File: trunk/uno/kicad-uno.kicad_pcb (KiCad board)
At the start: 2 copper layers, 57 parts, among them J1 RESET_EN, Q1 FDN340P, SW1 RESET, U1 NCP1117 5V, U2 LP2985-33DBVR, U3 ATMEGA16U2-MU(R), U5 LM358, X2 USB-MINI-AB

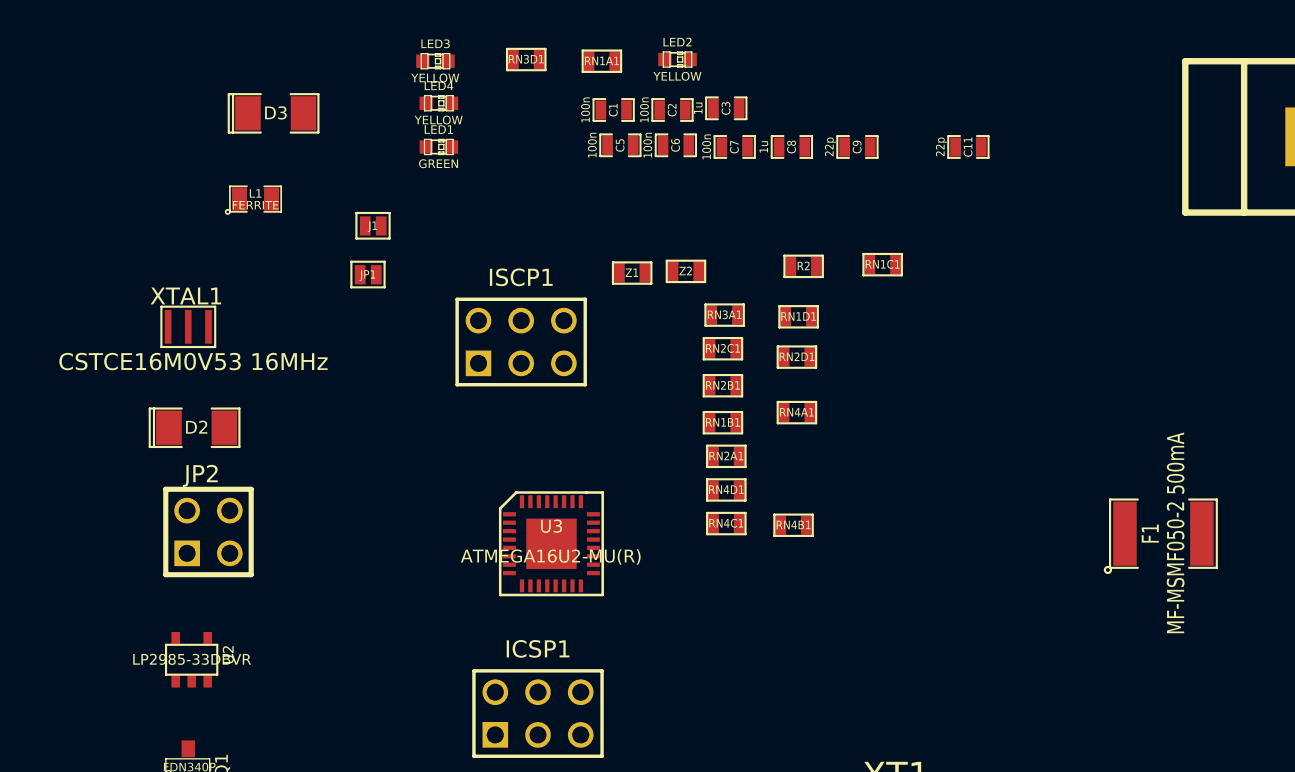
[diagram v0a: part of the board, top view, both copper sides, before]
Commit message: Added resistor network part/module for RN1-4 (no 3D package yet).
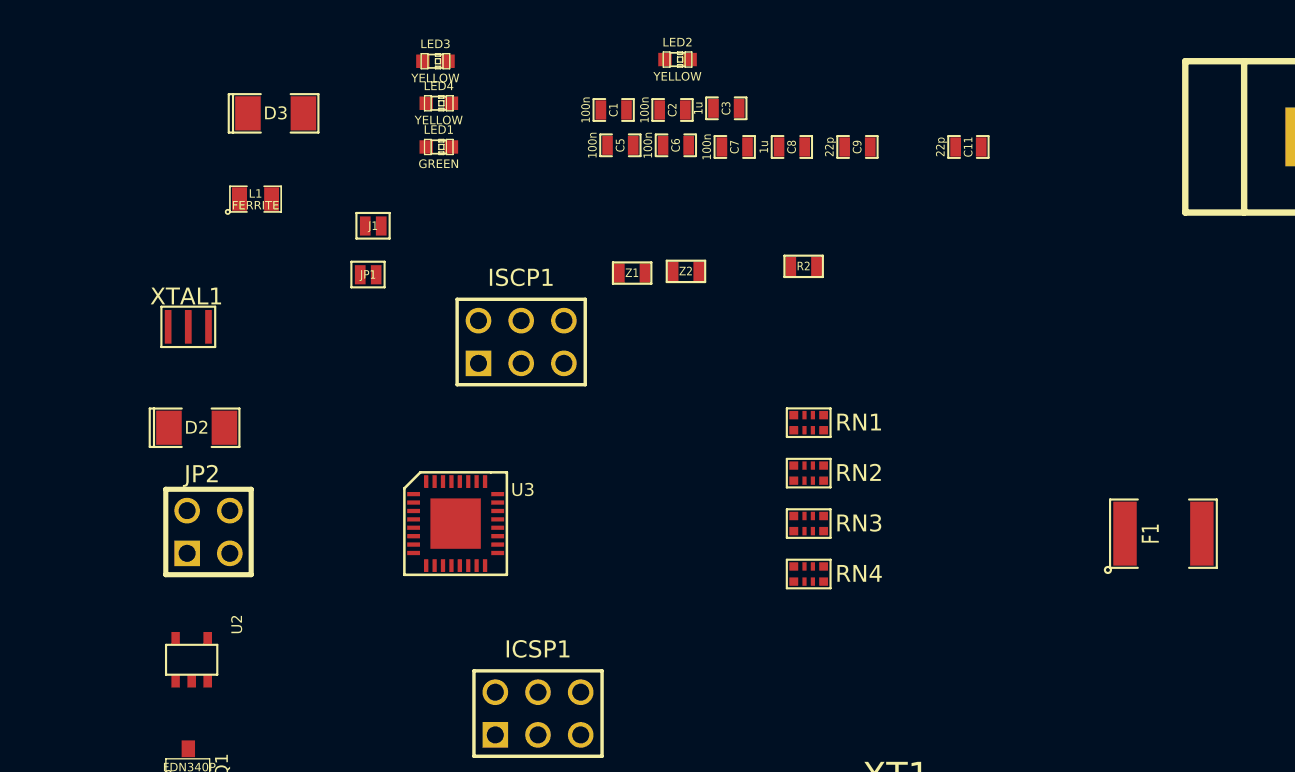
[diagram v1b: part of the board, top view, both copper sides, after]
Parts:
- removed RN1A1, RN1B1, RN1C1, RN1D1: 10K, SM0603
- removed RN2A1, RN2B1, RN2C1, RN2D1, RN4A1, RN4B1, RN4C1, RN4D1: 1K, SM0603
- removed RN3A1, RN3D1: 22R, SM0603
- added RN1: 10K, RN_EXB-28V, F.Cu at (17.0, 15.0)
- added RN2: 1K, RN_EXB-28V, F.Cu at (17.0, 18.0)
- added RN3: 22R, RN_EXB-28V, F.Cu at (17.0, 21.0)
- added RN4: 1K, RN_EXB-28V, F.Cu at (17.0, 24.0)
- moved U3 5.82 mm to (-4.00, 21.0)

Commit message: Board edges completed.
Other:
- board outline added: 68.6 x 53.3 mm
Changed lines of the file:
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@@
     (area 0 0 0 0)
     (thickness 1.6)
-    (drawings 0)
+    (drawings 12)
     (tracks 0)
     (zones 0)
@@
     (trace_min 0.254)
     (segment_width 0.127)
-    (edge_width 0.1)
+    (edge_width 0.254)
     (via_size 0.889)
     (via_drill 0.635)
@@
     (pad_drill 0)
     (pad_to_mask_clearance 0)
-    (aux_axis_origin 0 0)
+    (aux_axis_origin 25.4 25.4)
     (visible_elements 7FFFFBFF)
     (pcbplotparams
@@
     )
   )
+  (gr_arc (start 90.424 77.724) (end 91.44 77.724) (angle 90) (layer Edge.Cuts) (width 0.254))
+  (gr_arc (start 26.416 77.724) (end 26.416 78.74) (angle 90) (layer Edge.Cuts) (width 0.254))
+  (gr_arc (start 26.416 26.416) (end 25.4 26.416) (angle 90) (layer Edge.Cuts) (width 0.254))
+  (gr_line (start 25.4 77.724) (end 25.4 26.416) (angle 90) (layer Edge.Cuts) (width 0.254))
+  (gr_line (start 91.44 26.924) (end 89.916 25.4) (angle 90) (layer Edge.Cuts) (width 0.254))
+  (gr_line (start 91.44 38.354) (end 91.44 26.924) (angle 90) (layer Edge.Cuts) (width 0.254))
+  (gr_line (start 93.98 40.894) (end 91.44 38.354) (angle 90) (layer Edge.Cuts) (width 0.254))
+  (gr_line (start 93.98 73.66) (end 93.98 40.894) (angle 90) (layer Edge.Cuts) (width 0.254))
+  (gr_line (start 91.44 76.2) (end 93.98 73.66) (angle 90) (layer Edge.Cuts) (width 0.254))
+  (gr_line (start 91.44 77.724) (end 91.44 76.2) (angle 90) (layer Edge.Cuts) (width 0.254))
+  (gr_line (start 26.416 25.4) (end 89.916 25.4) (angle 90) (layer Edge.Cuts) (width 0.254))
+  (gr_line (start 26.416 78.74) (end 90.424 78.74) (angle 90) (layer Edge.Cuts) (width 0.254))
 )

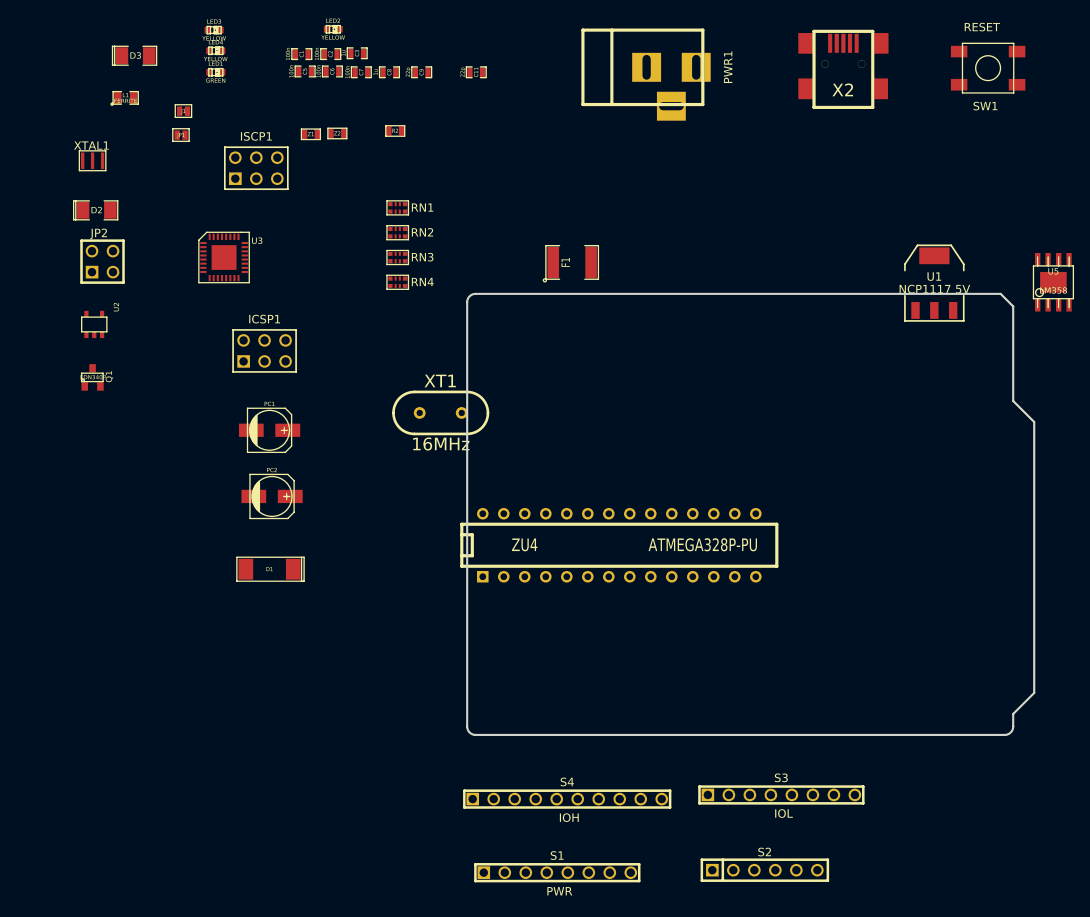
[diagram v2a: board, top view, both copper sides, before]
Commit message: About half the comoponents placed, in the exact same location as the UNO Rev3 reference design, except I changed the USB socket to a mini.
A number of minor schematic errors were corrected, around the pin 
numbering of the four resistor network chips.
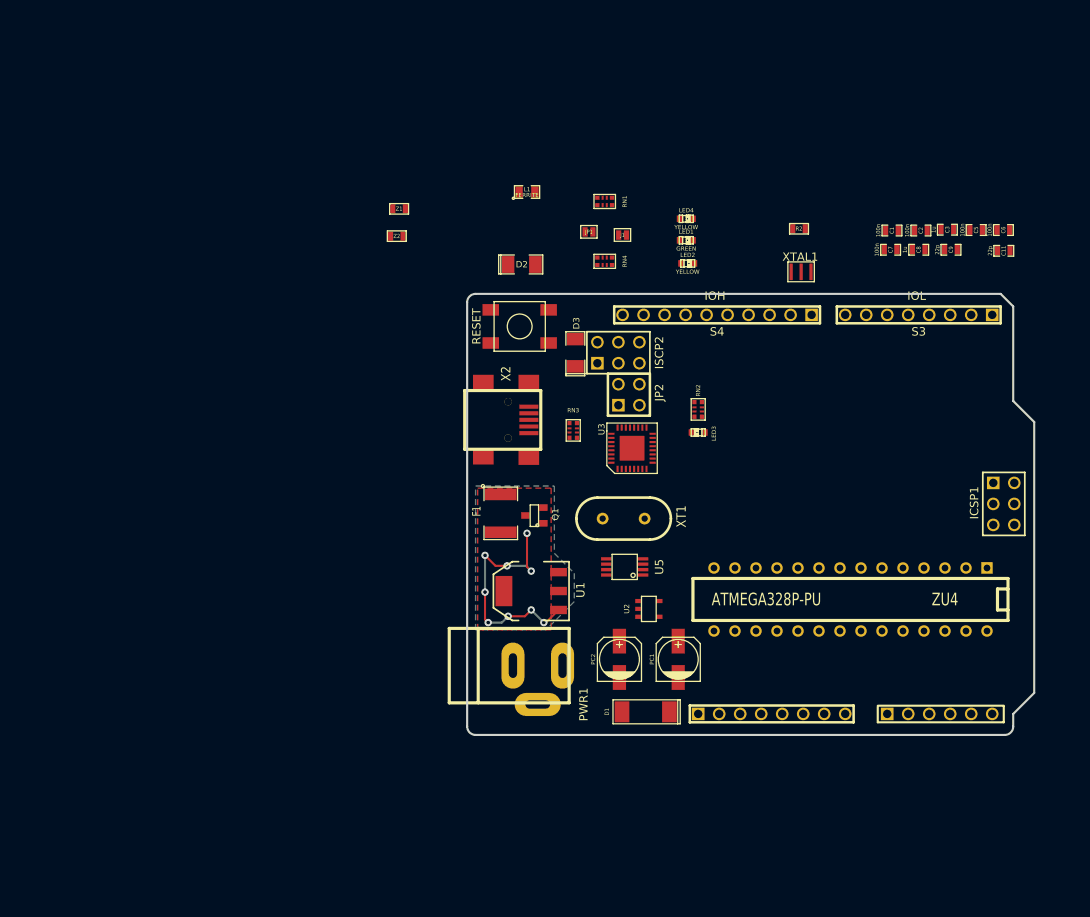
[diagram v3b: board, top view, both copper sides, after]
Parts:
- S2: footprint PIN_ARRAY-6X1 -> pin_array_6x1
- U5: footprint psop-8 -> SSOP8
- moved ICSP1 91.3 mm to (90.3, 50.8), turned to 270 degrees
- moved XTAL1 86.7 mm to (65.8, 22.7)
- moved C5 83.4 mm to (87.0, 17.7)
- moved C6 83.4 mm to (90.3, 17.7)
- moved LED3 76.1 mm to (53.3, 42.2), turned to 180 degrees
- moved U2 75.4 mm to (47.4, 63.5), turned to 270 degrees
- moved C3 74.5 mm to (83.5, 17.6)
- moved C1 74.5 mm to (76.8, 17.7)
- moved C2 74.5 mm to (80.3, 17.7)
- moved PWR1 74.1 mm to (30.7, 70.4)
- moved C7 67.5 mm to (76.6, 20.1)
- moved C9 67.5 mm to (83.9, 20.1)
- moved C8 67.5 mm to (80.0, 20.1)
- moved C11 67.4 mm to (90.3, 20.2)
- moved JP2 65.7 mm to (45.0, 37.6)
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- renumbered ISCP1 to ISCP2
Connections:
- PWR1 pad 1: GND -> N-0000040
- PWR1 pad 2: N-0000040 -> GND
- RN1 pad 1: VIN -> /POWER/CMP
- RN1 pad 3: /POWER/CMP -> +5V
- RN1 pad 4: GND -> /RESET
- RN1 pad 7: +5V -> GND
- RN1 pad 8: /RESET -> VIN
- RN2 pad 1: N-0000036 -> N-0000035
- RN2 pad 2: N-0000035 -> +5V
- RN2 pad 3: N-0000041 -> +5V
- RN2 pad 4: +5V -> DTR
- RN2 pad 5: N-0000042 -> GND
- RN2 pad 6: +5V -> N-0000042
- RN2 pad 7: DTR -> N-0000041
- RN2 pad 8: GND -> N-0000036
- RN3 pad 1: /USB/D- -> N-0000069
- RN3 pad 2: N-0000069 -> (no net)
- RN3 pad 4: (no net) -> N-0000068
- RN3 pad 5: (no net) -> /USB/D+
- RN3 pad 7: /USB/D+ -> (no net)
- RN3 pad 8: N-0000068 -> /USB/D-
- RN4 pad 2: TXD -> /IO0
- RN4 pad 3: /IO0 -> +5V
- RN4 pad 4: RXD -> +5V
- RN4 pad 5: +5V -> N-0000038
- RN4 pad 7: +5V -> RXD
- RN4 pad 8: N-0000038 -> TXD
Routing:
- net GND: track 0.00 -> 29.8 mm, vias 0 -> 9
- added copper zone on B.Cu, net GND
- added copper zone on F.Cu, net GND
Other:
- net class Default: clearance 0.254 -> 0.2032
- rule trace_clearance: 0.254 -> 0.2032

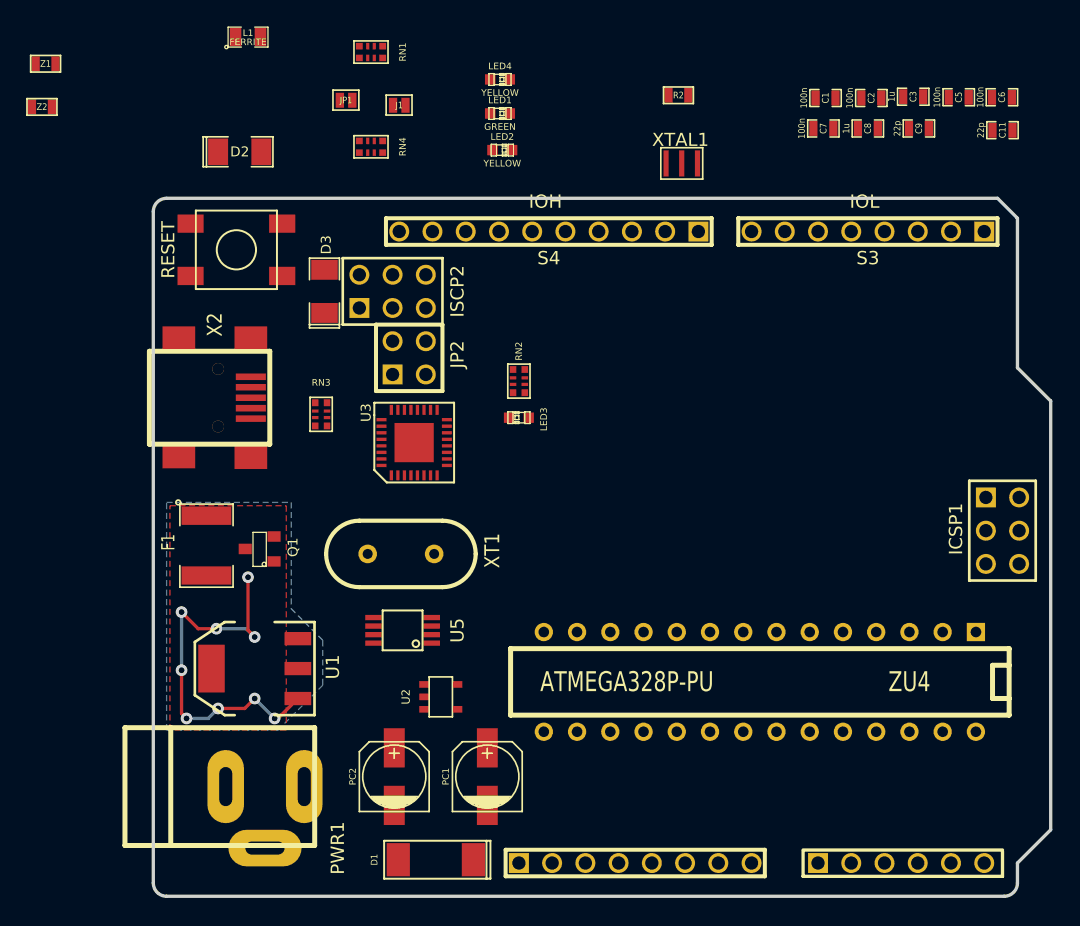
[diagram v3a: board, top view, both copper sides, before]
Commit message: All components placed. Some routing started.
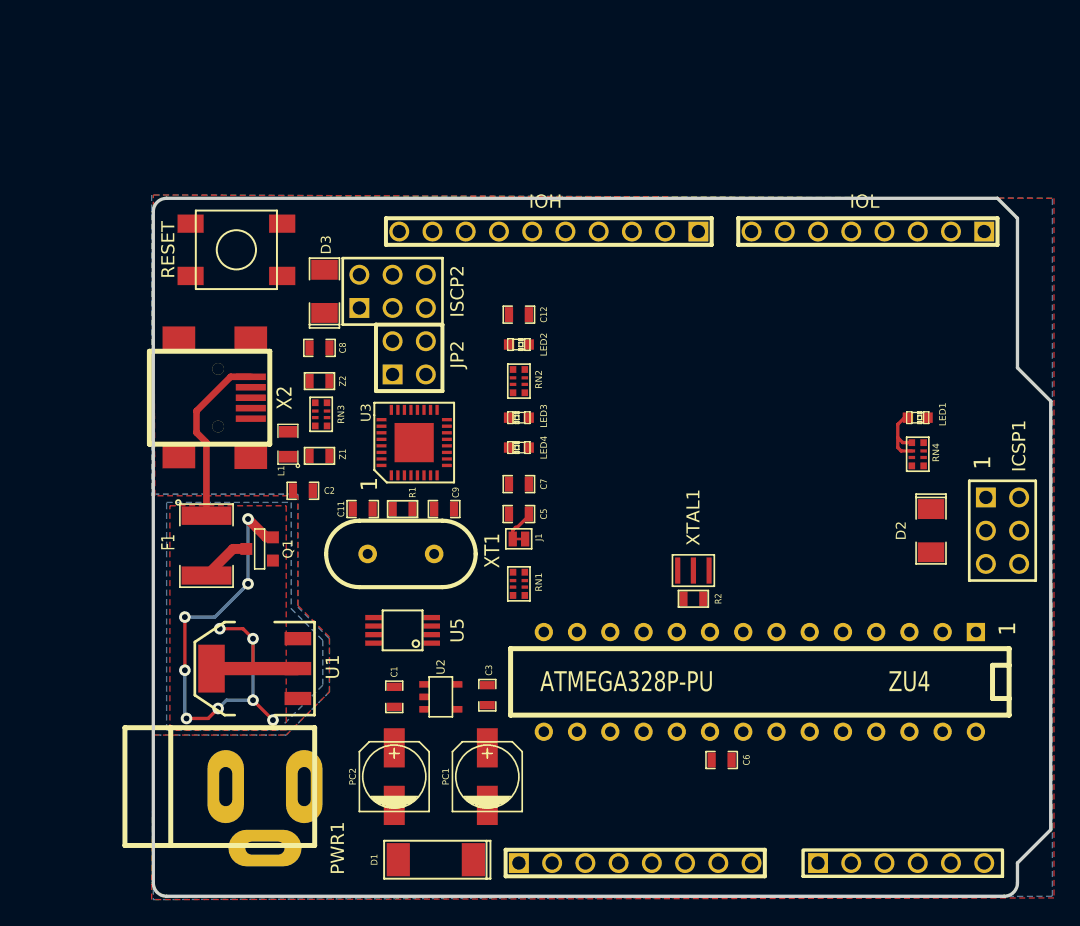
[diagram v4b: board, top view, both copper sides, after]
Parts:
- removed JP1: GROUND, JSOLD
- added C12: 100n, SM0603_Capa, F.Cu at (53.3, 34.3)
- added R1: 1M, SM0603, F.Cu at (44.5, 49.1)
- Q1: footprint SOT23 -> SOT23GDS
- moved D2 60.2 mm to (84.8, 50.8), turned to 270 degrees
- moved C11 56.8 mm to (41.4, 49.1)
- moved C1 56.4 mm to (43.8, 63.5), turned to 90 degrees
- moved C3 56.1 mm to (50.9, 63.4), turned to 270 degrees
- moved C6 55.0 mm to (68.8, 68.3)
- moved C2 52.8 mm to (36.8, 47.8)
- moved RN4 47.9 mm to (83.8, 45.0), turned to 90 degrees
- moved C9 46.5 mm to (47.6, 49.1)
- moved C5 46.3 mm to (53.3, 49.5)
- moved C8 45.1 mm to (38.1, 36.8), turned to 180 degrees
- moved RN1 42.2 mm to (53.3, 54.9), turned to 90 degrees
- moved LED1 39.5 mm to (83.8, 42.2)
- moved R2 38.5 mm to (66.7, 56.0)
- moved Z1 36.6 mm to (38.1, 45.1), turned to 180 degrees
- moved C7 35.8 mm to (53.3, 47.2)
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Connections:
- L1 pad 1: N-0000067 (its old number) -> GND
- L1 pad 2: GND -> N-0000058
- U3 pad 28: N-0000054 -> N-0000058
- X2 pad 5: GND -> N-0000058
- X2 pad 6: N-0000067 (its old number) -> GND
- X2 pad 7: N-0000067 (its old number) -> GND
- X2 pad 8: N-0000067 (its old number) -> GND
- X2 pad 9: N-0000067 (its old number) -> GND
- Z1 pad 2: N-0000067 (its old number) -> GND
- Z2 pad 2: N-0000067 (its old number) -> GND
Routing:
- net +5V: track 0.00 -> 45.4 mm, vias 0 -> 10
- net GND: track 29.8 -> 0.00 mm, vias 9 -> 0
- net N-0000065: track 0.00 -> 13.6 mm
- net N-0000038: track 0.00 -> 5.18 mm
- net USBVCC: track 0.00 -> 3.89 mm
- net /RESET: track 0.00 -> 3.44 mm
- added copper zone on B.Cu, net +5V
- added copper zone on F.Cu, net +5V
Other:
- rule trace_min: 0.254 -> 0.2032
- board text added: "1"

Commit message: More routing.
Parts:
- moved C2 1.20 mm to (37.5, 48.8)
- turned C11 to 180 degrees
- turned ISCP2 to 180 degrees
- turned JP2 to 90 degrees
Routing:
- net +5V: track 45.4 -> 231.7 mm, vias 10 -> 14
- net /AD5/SCL: track 0.00 -> 86.5 mm, vias 0 -> 3
- net /RESET: track 3.44 -> 86.0 mm, vias 0 -> 2
- net /AD4/SDA: track 0.00 -> 80.2 mm, vias 0 -> 3
- net AREF: track 0.00 -> 72.6 mm, vias 0 -> 1
- net GND: track 0.00 -> 66.6 mm, vias 0 -> 6
- net SCK: track 0.00 -> 65.7 mm, vias 0 -> 1
- net /USB/RESET2: track 0.00 -> 55.9 mm, vias 0 -> 2
- net N-000002: track 0.00 -> 50.7 mm, vias 0 -> 1
- net /IO9: track 0.00 -> 43.8 mm, vias 0 -> 1
- net N-000001: track 0.00 -> 42.8 mm, vias 0 -> 1
- net /SS: track 0.00 -> 42.0 mm, vias 0 -> 1
- net /IO7: track 0.00 -> 37.6 mm
- net /IO8: track 0.00 -> 37.0 mm
- net TXD: track 0.00 -> 36.7 mm
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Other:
- net class Power added: clearance 0.254, trace_width 0.508, via_dia 0.889, via_drill 0.635
